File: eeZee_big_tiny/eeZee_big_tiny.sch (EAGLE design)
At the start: 11 parts, among them IC1 ATtiny2313/4313, J2 avrisp, Q1 16MHz

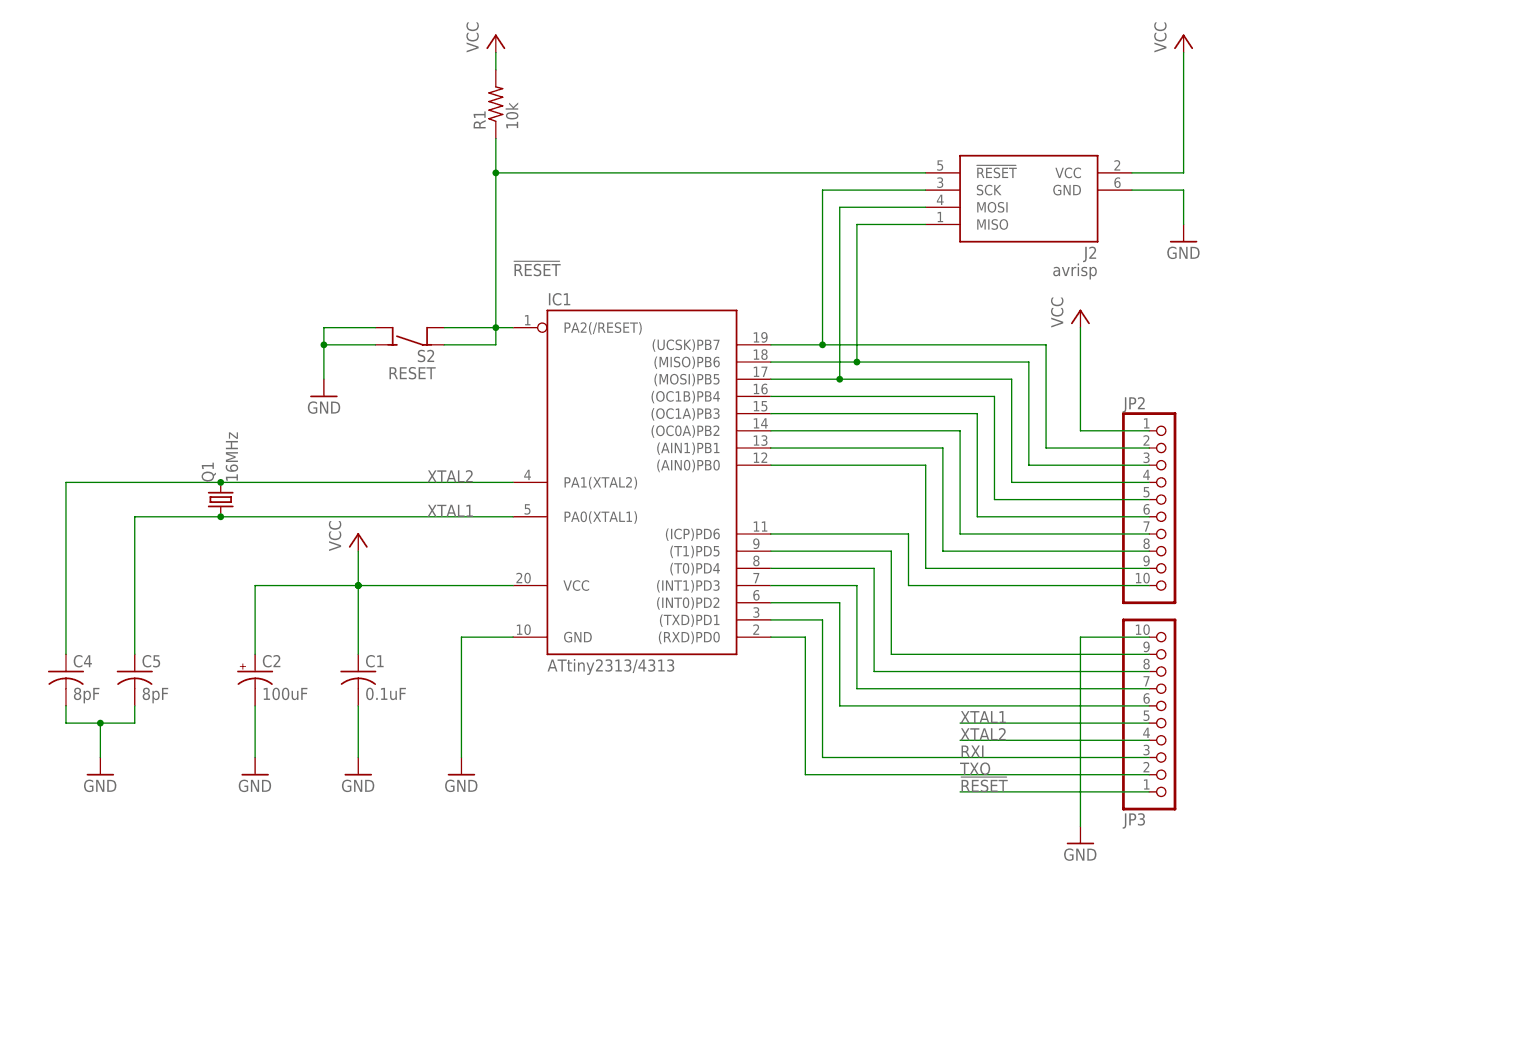
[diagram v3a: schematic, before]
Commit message: Revised board layout to match the new Tiny style, swapping in new reset button
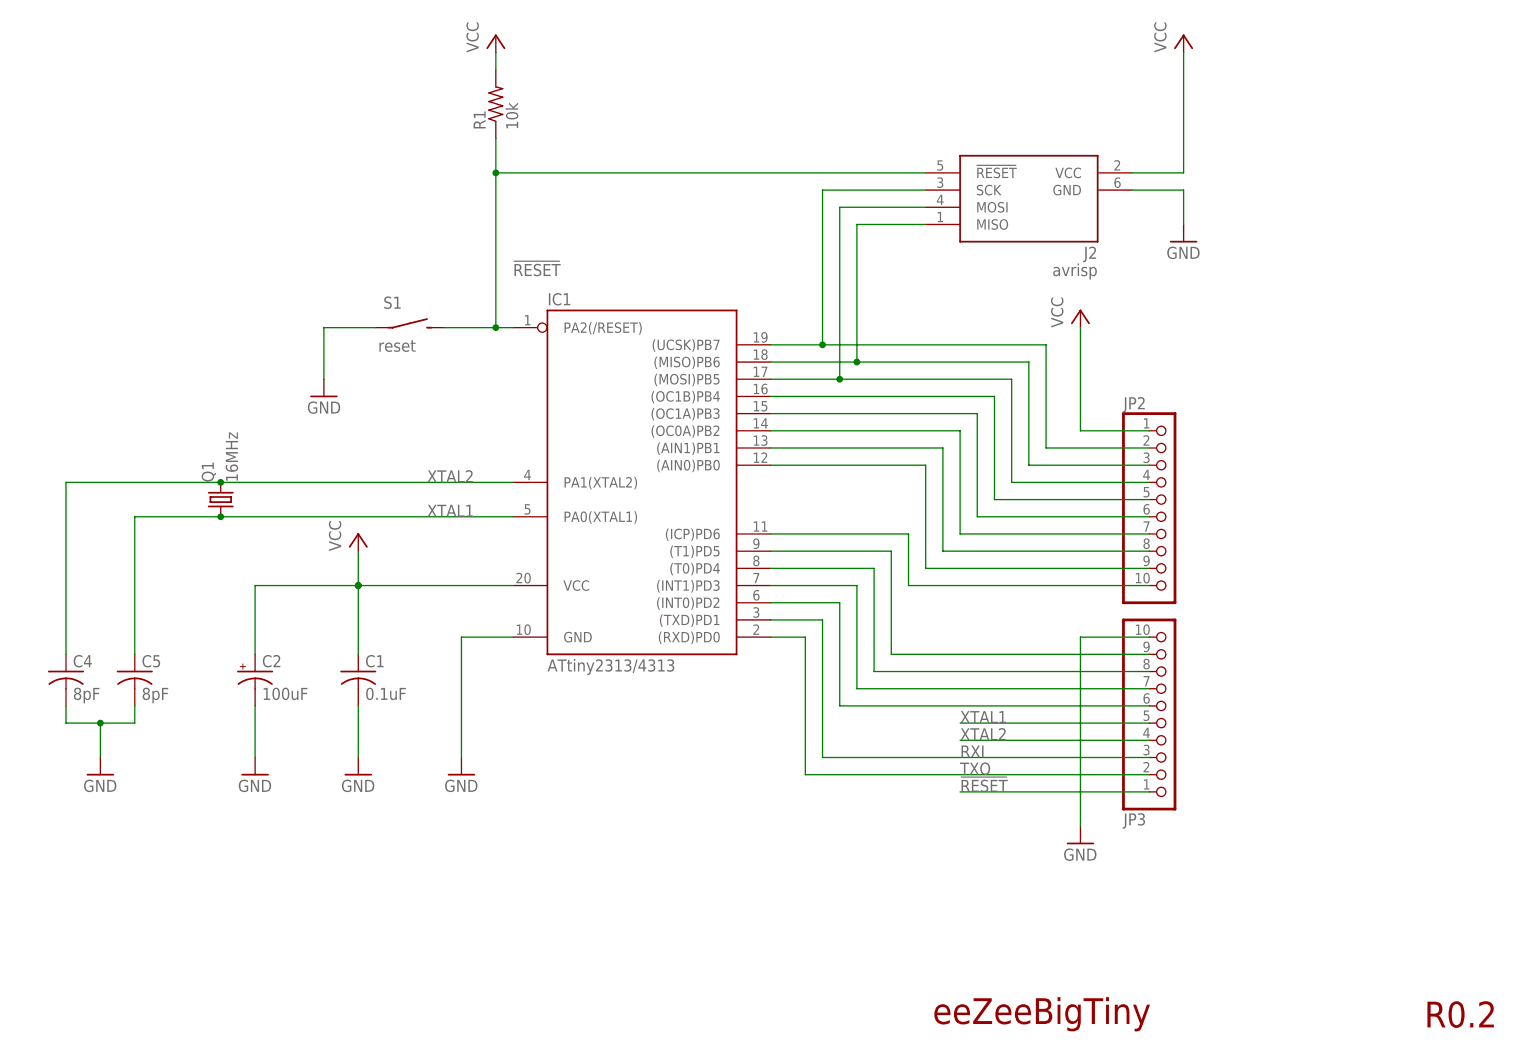
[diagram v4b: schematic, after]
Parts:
- removed S2: RESET, mes_electromech:SPST4
- added S1: reset, mes_electromech:SPST_TAC_RECT1
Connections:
- net !RESET: now also S1.S; no longer S2.COM@1, S2.COM@2
- net GND: now also S1.P; no longer S2.NO@1, S2.NO@2
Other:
- note added: "R0.2"
- note added: "eeZeeBigTiny"
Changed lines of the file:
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@@
 <?xml version="1.0" encoding="utf-8"?>
 <!DOCTYPE eagle SYSTEM "eagle.dtd">
-<eagle version="6.3">
+<eagle version="6.4">
 <drawing>
 <settings>
@@
 </part>
 <part name="J2" library="ads4" deviceset="AVRISP6" device="" value="avrisp"/>
-<part name="S2" library="mes_electromech" deviceset="SPST4" device="" value="RESET"/>
 <part name="IC1" library="avr-7" deviceset="TINY2313*" device="-*P*" value="ATtiny2313/4313"/>
 <part name="JP3" library="pinhead-2" deviceset="PINHD-1X10" device="_2.54-S"/>
@@
 </part>
 <part name="GND7" library="supply1" deviceset="GND" device=""/>
+<part name="S1" library="mes_electromech" deviceset="SPST" device="_TAC_RECT1" value="reset"/>
 </parts>
 <sheets>
 <sheet>
 <plain>
+<text x="158.496" y="24.13" size="3.81" layer="94">eeZeeBigTiny</text>
+<text x="231.14" y="23.622" size="3.81" layer="94">R0.2</text>
 </plain>
 <instances>
@@
 </instance>
 <instance part="J2" gate="A" x="172.72" y="142.24" rot="MR0"/>
-<instance part="S2" gate="G$1" x="81.28" y="124.46" rot="MR0"/>
 <instance part="IC1" gate="G$1" x="116.84" y="109.22"/>
 <instance part="JP3" gate="A" x="193.04" y="68.58" rot="MR180"/>
@@
 <instance part="P+4" gate="VCC" x="180.34" y="129.54"/>
 <instance part="FRAME1" gate="G$1" x="248.92" y="185.42" rot="R180"/>
-<instance part="FRAME1" gate="G$2" x="248.92" y="27.94" rot="R180"/>
+<instance part="FRAME1" gate="G$2" x="147.32" y="2.54"/>
 <instance part="GND5" gate="1" x="73.66" y="60.96"/>
 <instance part="GND6" gate="1" x="58.42" y="60.96"/>
@@
 </instance>
 <instance part="GND7" gate="1" x="35.56" y="60.96"/>
+<instance part="S1" gate="G$1" x="81.28" y="127"/>
 </instances>
 <busses>
@@
 </segment>
 <segment>
-<wire x1="68.58" y1="119.38" x2="68.58" y2="124.46" width="0.1524" layer="91"/>
+<wire x1="68.58" y1="119.38" x2="68.58" y2="127" width="0.1524" layer="91"/>
 <pinref part="GND3" gate="1" pin="GND"/>
-<pinref part="S2" gate="G$1" pin="NO@1"/>
-<pinref part="S2" gate="G$1" pin="NO@2"/>
-<wire x1="68.58" y1="124.46" x2="76.2" y2="124.46" width="0.1524" layer="91"/>
-<wire x1="76.2" y1="127" x2="68.58" y2="127" width="0.1524" layer="91"/>
-<wire x1="68.58" y1="127" x2="68.58" y2="124.46" width="0.1524" layer="91"/>
-<junction x="68.58" y="124.46"/>
+<wire x1="68.58" y1="127" x2="76.2" y2="127" width="0.1524" layer="91"/>
+<pinref part="S1" gate="G$1" pin="P"/>
 </segment>
 <segment>
@@
 <junction x="93.98" y="149.86"/>
 <pinref part="R1" gate="G$1" pin="1"/>
-<wire x1="86.36" y1="124.46" x2="93.98" y2="124.46" width="0.1524" layer="91"/>
+<wire x1="86.36" y1="127" x2="93.98" y2="127" width="0.1524" layer="91"/>
 <pinref part="J2" gate="A" pin="!RESET"/>
-<pinref part="S2" gate="G$1" pin="COM@1"/>
-<pinref part="S2" gate="G$1" pin="COM@2"/>
-<wire x1="86.36" y1="127" x2="93.98" y2="127" width="0.1524" layer="91"/>
 <junction x="93.98" y="127"/>
 <pinref part="IC1" gate="G$1" pin="PA2(/RESET)"/>
 <wire x1="96.52" y1="127" x2="93.98" y2="127" width="0.1524" layer="91"/>
-<wire x1="93.98" y1="124.46" x2="93.98" y2="127" width="0.1524" layer="91"/>
 <wire x1="93.98" y1="149.86" x2="93.98" y2="127" width="0.1524" layer="91"/>
 <label x="96.52" y="134.62" size="1.778" layer="95"/>
-</segment>
-<segment>
+<pinref part="S1" gate="G$1" pin="S"/>
+</segment>
+<segment>

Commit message: Rev 0.2, mitered corners, changed silk on tantalum to indicate polarity, few minor rearrangements.
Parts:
- C2: device rcl:CPOL-USSMCB -> mes_rcl:CAP_POL_SMC_B
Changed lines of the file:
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@@
 <part name="GND5" library="supply1" deviceset="GND" device=""/>
 <part name="GND6" library="supply1" deviceset="GND" device=""/>
-<part name="C2" library="rcl" deviceset="CPOL-US" device="SMCB" value="100uF">
+<part name="C2" library="mes_rcl" deviceset="CAP_POL" device="_SMC_B" value="100uF">
 <attribute name="BOM" value="EXCLUDE"/>
 <attribute name="PARTNO" value="MCTT21X106M6R3CT"/>
